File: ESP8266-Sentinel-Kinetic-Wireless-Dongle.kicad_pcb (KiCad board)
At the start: 2 copper layers, 39.7 x 59.9 mm, 55 parts, among them J1 Conn_01x04, J2 Screw_Terminal_01x04, J3 Conn_01x06_Pin, J4 RJ9, J5 Screw_Terminal_01x03, J6 Screw_Terminal_01x02, Q1 AO3400A, SW2 SW_Push, SW4 SW_Push, U1 AMS1117-3.3, U2 ESP-12F, U3 MAX3232, U4 ESP32-WROOM-32, U5 L78L12_SOT89, U6 PC817

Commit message: Added PDF and OSHW logo
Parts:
- added REF**: OSHW-Logo2_7.3x6mm_SilkScreen, Symbol:OSHW-Logo2_7.3x6mm_SilkScreen, F.Cu at (164.4, 109.5)

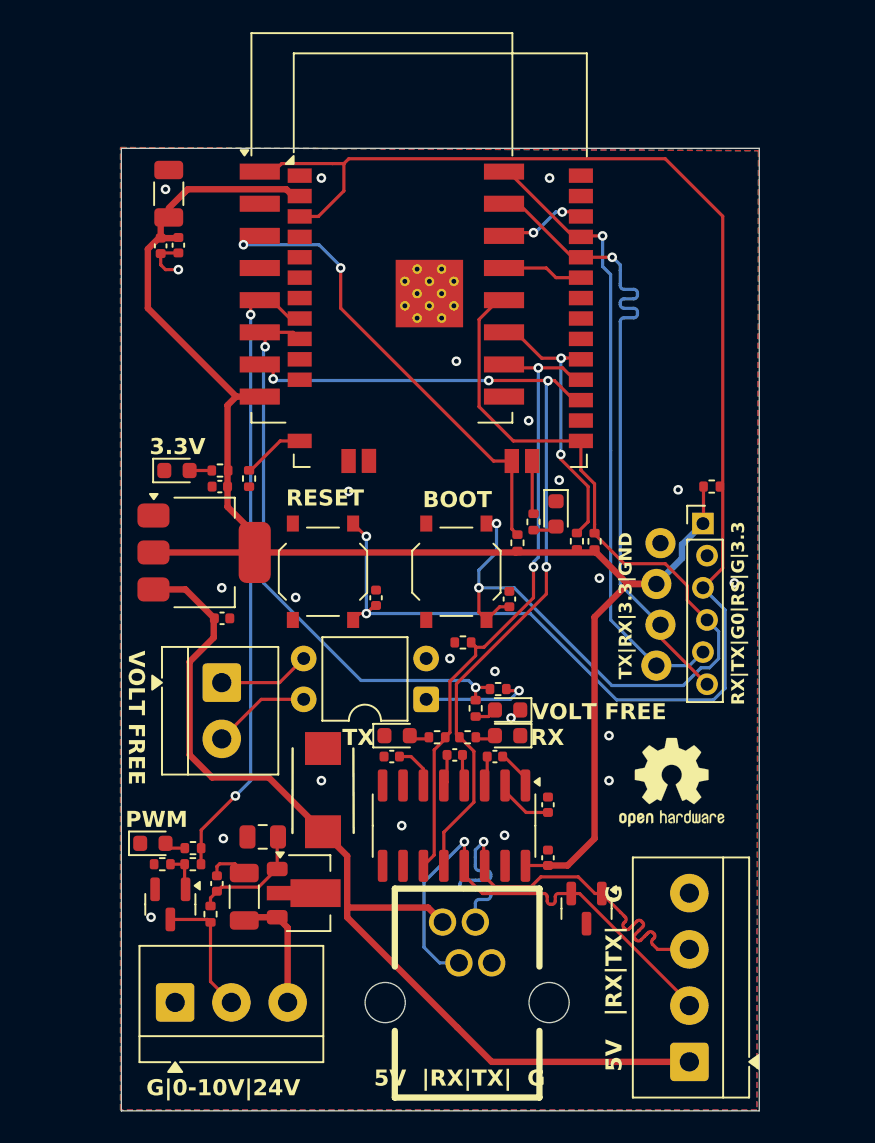
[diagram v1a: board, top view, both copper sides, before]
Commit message: Completed PCB Layout Added PWM Rail to rail Added Silkscreen markings
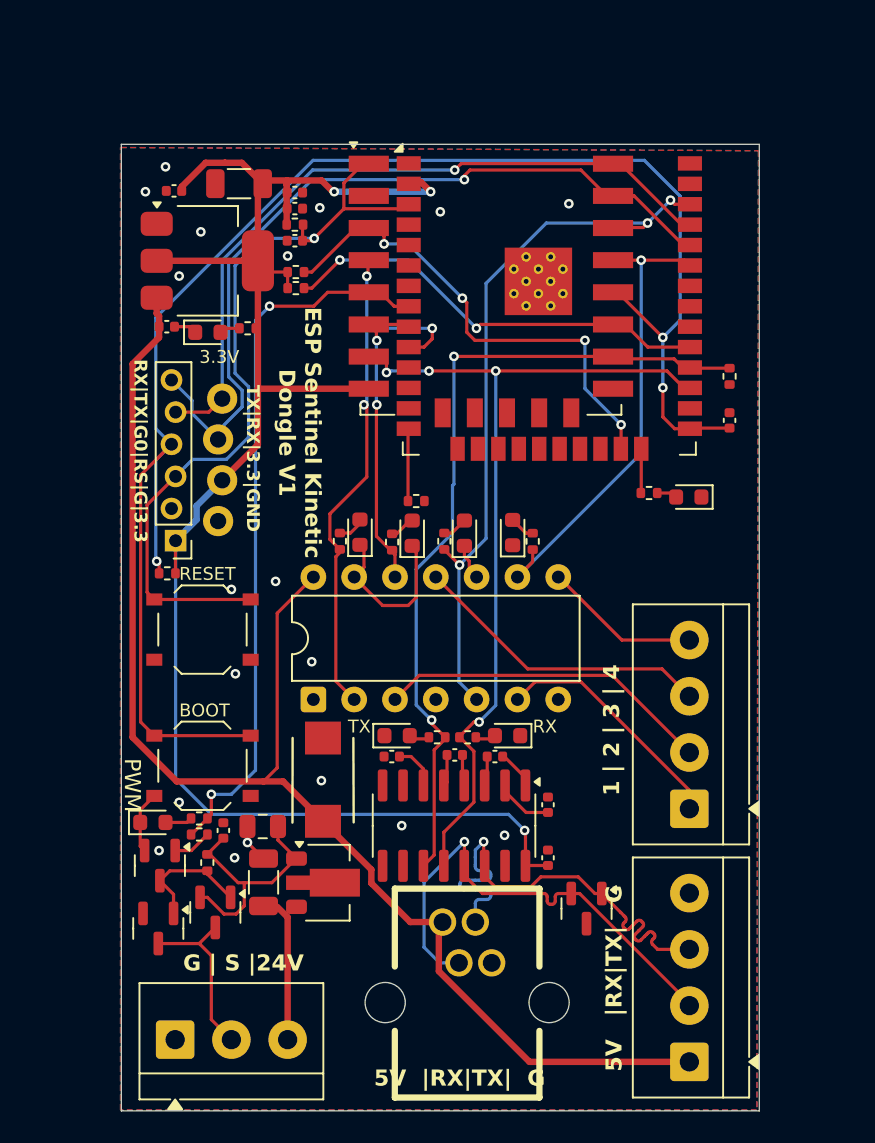
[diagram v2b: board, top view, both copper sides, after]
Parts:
- removed R15: 10K, Resistor_SMD:R_0402_1005Metric
- removed REF**: OSHW-Logo2_7.3x6mm_SilkScreen, Symbol:OSHW-Logo2_7.3x6mm_SilkScreen
- added D10: LED, LED_SMD:LED_0603_1608Metric, F.Cu at (148.2, 94.0)
- added D11: LED, LED_SMD:LED_0603_1608Metric, F.Cu at (145.0, 93.9)
- added D9: LED, LED_SMD:LED_0603_1608Metric, F.Cu at (151.5, 94.0)
- added Q2: AO3401A, Package_TO_SOT_SMD:SOT-23, F.Cu at (136.0, 117.6)
- added Q3: AO3400A, Package_TO_SOT_SMD:SOT-23, F.Cu at (132.4, 118.6)
- added R13: 1K, Resistor_SMD:R_0402_1005Metric, F.Cu at (150.2, 94.5)
- added R18: 1K, Resistor_SMD:R_0402_1005Metric, F.Cu at (143.8, 94.5)
- J6: value Screw_Terminal_01x02 -> Screw_Terminal_01x04; footprint TerminalBlock_4Ucon:TerminalBlock_4Ucon_1x02_P3.50mm_Horizontal -> TerminalBlock_4Ucon:TerminalBlock_4Ucon_1x04_P3.50mm_Horizontal
- Q1: value AO3400A -> SS8050
- U2: value ESP-12F -> ESP-12E
- U5: value L78L12_SOT89 -> L78L10_SOT89
- U6: value PC817 -> 74AHCT125; footprint Package_DIP:DIP-4_W7.62mm -> Package_DIP:DIP-14_W7.62mm
- moved J3 33.1 mm to (133.4, 94.5), turned to 180 degrees
- moved R4 30.6 mm to (140.9, 74.8)
- moved J6 30.1 mm to (165.5, 111.2), turned to 90 degrees
- moved J1 27.3 mm to (136.3, 93.2), turned to 90 degrees
- moved R3 26.7 mm to (133.0, 96.5), turned to 180 degrees
- moved R1 23.5 mm to (141.0, 78.8), turned to 0 degrees
- moved R5 23.4 mm to (168.0, 84.2), turned to 90 degrees
- moved C5 22.8 mm to (140.9, 75.8), turned to 180 degrees
- moved R2 21.8 mm to (141.0, 77.8), turned to 0 degrees
- moved SW2 19.9 mm to (135.2, 108.5), turned to 0 degrees
- moved C2 18.6 mm to (133.4, 72.7)
- moved C1 18.5 mm to (133.0, 81.2)
- moved U1 18.2 mm to (135.5, 77.0)
- moved C6 17.6 mm to (168.0, 87.0)
- moved R17 11.3 mm to (147.0, 94.5), turned to -90 degrees
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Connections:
- Q1 pad 1: Net-(Q1-G) -> Net-(Q1-B)
- Q1 pad 3: /10V_PWM -> Net-(Q1-C)
- R12 pad 2: /OPTO -> /OUT1
- R14 pad 1: Net-(Q1-G) -> /PWM
- R14 pad 2: /PWM -> Net-(Q1-B)
- R16 pad 2: /10V_PWM -> Net-(Q1-C)
- R17 pad 1: Net-(R17-Pad1) -> Net-(D10-A)
- R17 pad 2: /OPTO -> /OUT3
- U2 pad 19: /SDA -> /OUT1
- U2 pad 20: /SCL -> /OUT2
- U2 pad 4: unconnected-(U2-GPIO16-Pad4) -> /OUT4
- U2 pad 6: /OPTO -> /OUT3
- U4 pad 10: unconnected-(U4-IO25-Pad10) -> /OUT4
- U4 pad 33: /SDA -> /OUT1
- U4 pad 36: /SCL -> /OUT2
- U4 pad 9: /OPTO -> /OUT3
- U6 pad 1: Net-(R17-Pad1) -> GND
- U6 pad 2: GND -> /OUT4
- U6 pad 3: Net-(J6-Pin_1) -> Net-(J6-Pin_2)
- U6 pad 4: Net-(J6-Pin_2) -> GND
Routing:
- net /RST: track 98.8 -> 49.0 mm, vias 2 -> 1
- net /OUT2: track 0.00 -> 45.6 mm, vias 0 -> 3
- net /GPIO0: track 60.5 -> 102.6 mm, vias 2 -> 3
- net /OPTO: track 36.1 -> 0.00 mm, vias 2 -> 0
- net /OUT4: track 0.00 -> 35.8 mm, vias 0 -> 3
- net /OUT1: track 0.00 -> 29.9 mm, vias 0 -> 1
- net +5V: track 61.2 -> 88.1 mm
- net /OUT3: track 0.00 -> 19.0 mm, vias 0 -> 2
- net Net-(J6-Pin_3): track 0.00 -> 18.9 mm
- net Net-(J6-Pin_2): track 6.12 -> 20.9 mm
- net GND: track 5.35 -> 19.4 mm, vias 23 -> 19
- net /ALT_TX: track 40.2 -> 51.4 mm
- net /SH_1: track 17.4 -> 27.2 mm
- net Net-(J6-Pin_4): track 0.00 -> 9.78 mm
- net /RX: track 40.5 -> 50.0 mm
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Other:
- board size 39.7 x 59.9 mm -> 39.7 x 60.1 mm
- board text added: "1 | 2 | 3 | 4"
- board text added: "ESP Sentinel Kinetic Dongle V1"
- board text added: "G | S |24V"
- board text removed: "G|0-10V|24V"
- board text removed: "VOLT FREE"

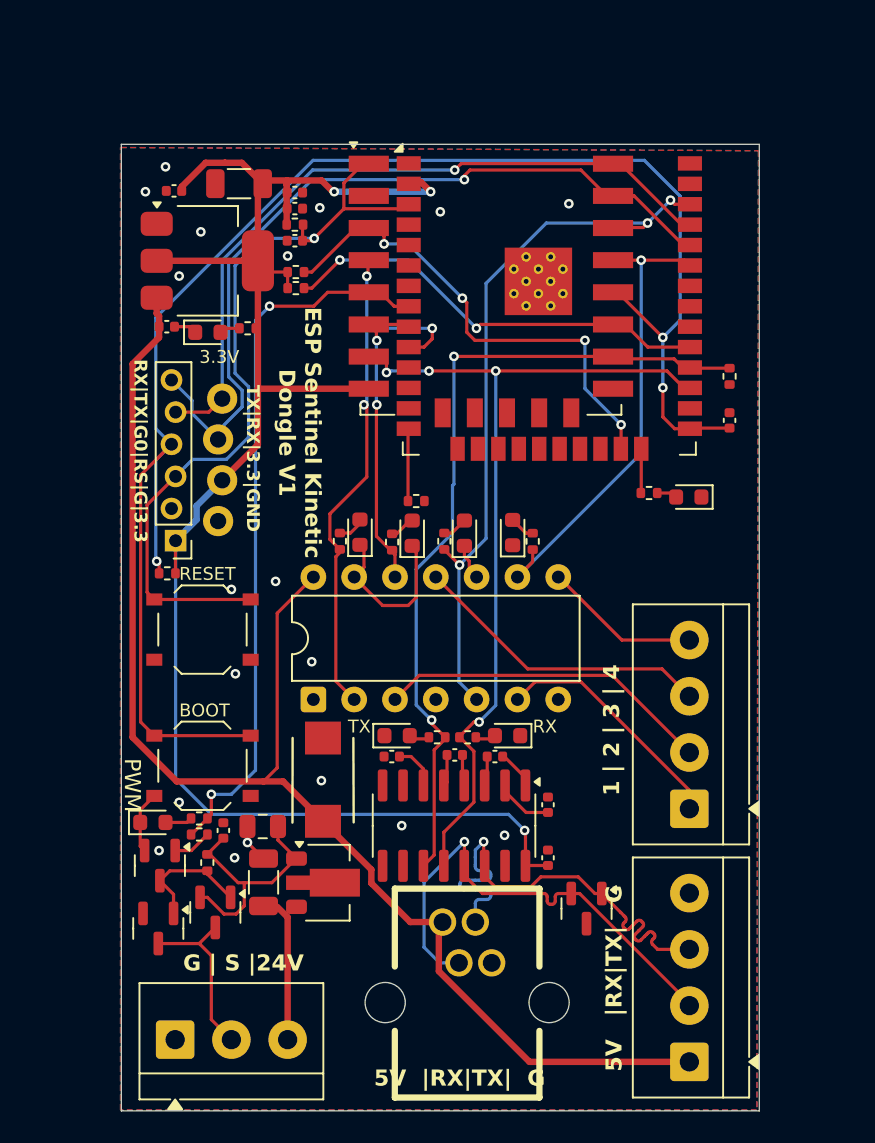
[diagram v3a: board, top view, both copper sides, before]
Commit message: corrected rx and tx positions for lilygo downloader
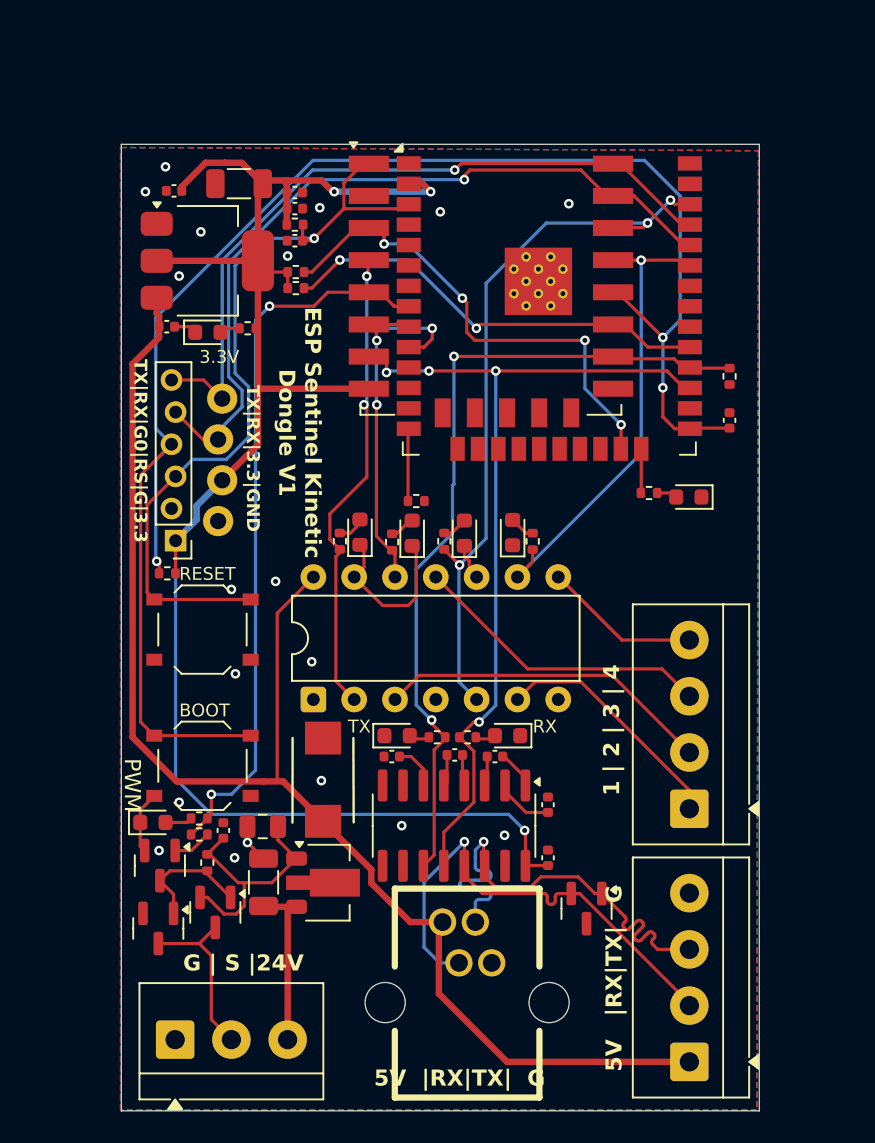
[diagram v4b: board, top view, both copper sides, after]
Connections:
- J3 pad 5: /TX -> /RX
- J3 pad 6: /RX -> /TX
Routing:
- net /RX: track 50.0 -> 48.5 mm
- net +5V: track 88.1 -> 89.4 mm
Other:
- board text added: "TX|RX|G0|RS|G|3.3"
- board text removed: "RX|TX|G0|RS|G|3.3"
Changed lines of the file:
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@@
 			(layers "*.Cu" "*.Mask")
 			(remove_unused_layers no)
-			(net 21 "/TX")
+			(net 20 "/RX")
 			(pinfunction "Pin_5")
 			(pintype "passive")
@@
 			(layers "*.Cu" "*.Mask")
 			(remove_unused_layers no)
-			(net 20 "/RX")
+			(net 21 "/TX")
 			(pinfunction "Pin_6")
 			(pintype "passive")
@@
 		)
 	)
-	(gr_text "RX|TX|G0|RS|G|3.3"
+	(gr_text "TX|RX|G0|RS|G|3.3"
 		(at 130.873 83.1673 270)
 		(layer "F.SilkS")
@@
 	)
 	(segment
-		(start 150.14 118.2)
-		(end 149.909 118.431)
+		(start 145.709 115.782388)
+		(end 148.126612 118.2)
 		(width 0.4)
 		(layer "F.Cu")
@@
 	)
 	(segment
-		(start 145.709 115.782388)
-		(end 148.126612 118.2)
+		(start 149.909 122.659)
+		(end 154.15 126.9)
 		(width 0.4)
 		(layer "F.Cu")
@@
 	)
 	(segment
-		(start 139.85 98.98)
-		(end 139.85 108.6)
-		(width 0.2)
+		(start 142.7 111.93)
+		(end 145.709 114.939)
+		(width 0.4)
 		(layer "F.Cu")
 		(net 2)
 	)
 	(segment
-		(start 155.550818 126.9)
-		(end 165.5 126.9)
+		(start 142.7 112.2)
+		(end 142.7 112.58)
 		(width 0.4)
 		(layer "F.Cu")
@@
 	)
 	(segment
-		(start 149.909 121.258182)
-		(end 155.550818 126.9)
+		(start 145.709 114.939)
+		(end 145.709 115.782388)
 		(width 0.4)
 		(layer "F.Cu")
@@
 	)
 	(segment
-		(start 142.7 111.93)
-		(end 145.709 114.939)
+		(start 154.15 126.9)
+		(end 165.5 126.9)
 		(width 0.4)
 		(layer "F.Cu")
@@
 	)
 	(segment
-		(start 142.1 96.73)
-		(end 139.85 98.98)
-		(width 0.2)
+		(start 139.001 109.449)
+		(end 140.219 109.449)
+		(width 0.4)
 		(layer "F.Cu")
 		(net 2)
 	)
 	(segment
-		(start 142.7 112.2)
-		(end 142.7 112.58)
+		(start 150.14 118.2)
+		(end 149.909 118.431)
 		(width 0.4)
 		(layer "F.Cu")
@@
 	)
 	(segment
-		(start 139.85 108.6)
-		(end 139.001 109.449)
+		(start 139.85 98.98)
+		(end 139.85 109.349)
 		(width 0.2)
 		(layer "F.Cu")
@@
 	)
 	(segment
-		(start 145.709 114.939)
-		(end 145.709 115.782388)
-		(width 0.4)
-		(layer "F.Cu")
-		(net 2)
-	)
-	(segment
-		(start 139.001 109.449)
-		(end 140.219 109.449)
+		(start 132.5 81.82)
+		(end 130.851 83.469)
 		(width 0.4)
 		(layer "F.Cu")
@@
 	(segment
 		(start 149.909 118.431)
-		(end 149.909 121.258182)
+		(end 149.909 122.659)
 		(width 0.4)
 		(layer "F.Cu")
@@
 	)
 	(segment
-		(start 132.5 81.82)
-		(end 130.851 83.469)
-		(width 0.4)
+		(start 142.1 96.73)
+		(end 139.85 98.98)
+		(width 0.2)
 		(layer "F.Cu")
 		(net 2)
@@
 	)
 	(segment
+		(start 139.75 109.449)
+		(end 139.001 109.449)
+		(width 0.2)
+		(layer "F.Cu")
+		(net 2)
+	)
+	(segment
 		(start 132.35 80.33)
 		(end 132.5 80.48)
@@
 	)
 	(segment
+		(start 139.85 109.349)
+		(end 139.75 109.449)
+		(width 0.2)
+		(layer "F.Cu")
+		(net 2)
+	)
+	(segment
 		(start 139.15 72.05)
 		(end 138.95 72.25)
@@
 	)
 	(segment
+		(start 135.227 88.1673)
+		(end 136.173 88.1673)
+		(width 0.2)
+		(layer "F.Cu")
+		(net 20)
+	)
+	(segment
 		(start 165.12 76.07)
 		(end 165.535 76.07)
@@
 	)
 	(segment
+		(start 133.527 86.4673)
+		(end 135.227 88.1673)
+		(width 0.2)
+		(layer "F.Cu")
+		(net 20)
+	)
+	(segment
 		(start 151.849 71.401)
 		(end 158.751 71.401)
@@
 	)
 	(segment
-		(start 134.55 85.7443)
-		(end 134.55 86.5443)
-		(width 0.2)
-		(layer "B.Cu")
-		(net 20)
-	)
-	(segment
 		(start 136.828 77.1891)
 		(end 136.828 84.273543)
@@
 	)
 	(segment
-		(start 133.273 84.4673)
-		(end 134.55 85.7443)
-		(width 0.2)
-		(layer "B.Cu")
-		(net 20)
-	)
-	(segment
-		(start 134.55 86.5443)
-		(end 136.173 88.1673)
-		(width 0.2)
-		(layer "B.Cu")
-		(net 20)
-	)
-	(segment
 		(start 136.828 84.273543)
 		(end 137.6678 85.113343)
@@
 	)
 	(segment
-		(start 133.527 86.4673)
-		(end 135.587 86.4673)
+		(start 150.9 71.4)
+		(end 151.3 71)
 		(width 0.2)
 		(layer "F.Cu")
@@
 	)
 	(segment
-		(start 150.9 71.4)
-		(end 151.3 71)
+		(start 135.267 84.4673)
+		(end 136.427 85.6273)
 		(width 0.2)
 		(layer "F.Cu")
@@
 	)
 	(segment
-		(start 135.587 86.4673)
-		(end 136.427 85.6273)
+		(start 133.273 84.4673)
+		(end 135.267 84.4673)
 		(width 0.2)
 		(layer "F.Cu")
@@
 	)
 	(segment
-		(start 140.5 117.9)
-		(end 140.5 125.5175)
+		(start 139.85 117.25)
+		(end 140.5 117.25)
 		(width 0.4)
 		(layer "F.Cu")
@@
 	)
 	(segment
-		(start 139.85 117.25)
-		(end 140.5 117.9)
+		(start 140.5 117.25)
+		(end 140.5 125.5175)
 		(width 0.4)
 		(layer "F.Cu")
@@
 	)
 	(group ""
-		(members "7330ef8c-6481-4db9-bce3-4992c653ba21" "ad0d92fb-31f8-4e88-ba23-8c2adcbaf2d2")
-	)
-	(group ""
-		(members "1da7c134-e7de-46f6-986a-f2590a6dd704" "36b0c2f8-dcde-4590-90a0-c55bb1c2abd9"
-			"64731af3-c0c0-4930-88bb-ad1b50b03f91"
-		)
+		(members "ad0d92fb-31f8-4e88-ba23-8c2adcbaf2d2")
 	)
 	(generated

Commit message: Added Silkscreen markings to Diagnostic LED's Inverted Serial LED's, so LED is only on when signal is sent or recieved.
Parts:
- moved R6 8.04 mm to (156.5, 92.8)
- moved D4 7.56 mm to (158.2, 94.0), turned to 90 degrees
- moved R8 4.02 mm to (159.5, 93.5), turned to 90 degrees
- turned D5 to 0 degrees
- turned D6 to 180 degrees
- turned R10 to 180 degrees
- turned R9 to 0 degrees
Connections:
- D5 pad 1: GND -> Net-(D5-K)
- D5 pad 2: Net-(D5-A) -> +3.3V
- D6 pad 1: GND -> Net-(D6-K)
- D6 pad 2: Net-(D6-A) -> +3.3V
- R10 pad 1: Net-(D6-A) -> /ALT_TX
- R10 pad 2: /ALT_TX -> Net-(D6-K)
- R9 pad 1: Net-(D5-A) -> /ALT_RX
- R9 pad 2: /ALT_RX -> Net-(D5-K)
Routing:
- net +3.3V: track 106.0 -> 118.3 mm, vias 3 -> 5
- net /SL_1: track 4.31 -> 12.6 mm
- net /LED: track 2.76 -> 5.48 mm
- net Net-(D6-K): track 0.00 -> 1.51 mm
- net Net-(D5-K): track 0.00 -> 1.51 mm
- net Net-(D6-A): track 1.27 -> 0.00 mm
- net Net-(D5-A): track 1.27 -> 0.00 mm
- net GND: vias 19 -> 21
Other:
- board text added: "4 | 3 | 2 | 1 | IO2"
